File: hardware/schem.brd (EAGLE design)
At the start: 59.4 x 52.7 mm, 18 parts, among them IC1 7805L, IC2 L298, U2 TINY85-20-DIP

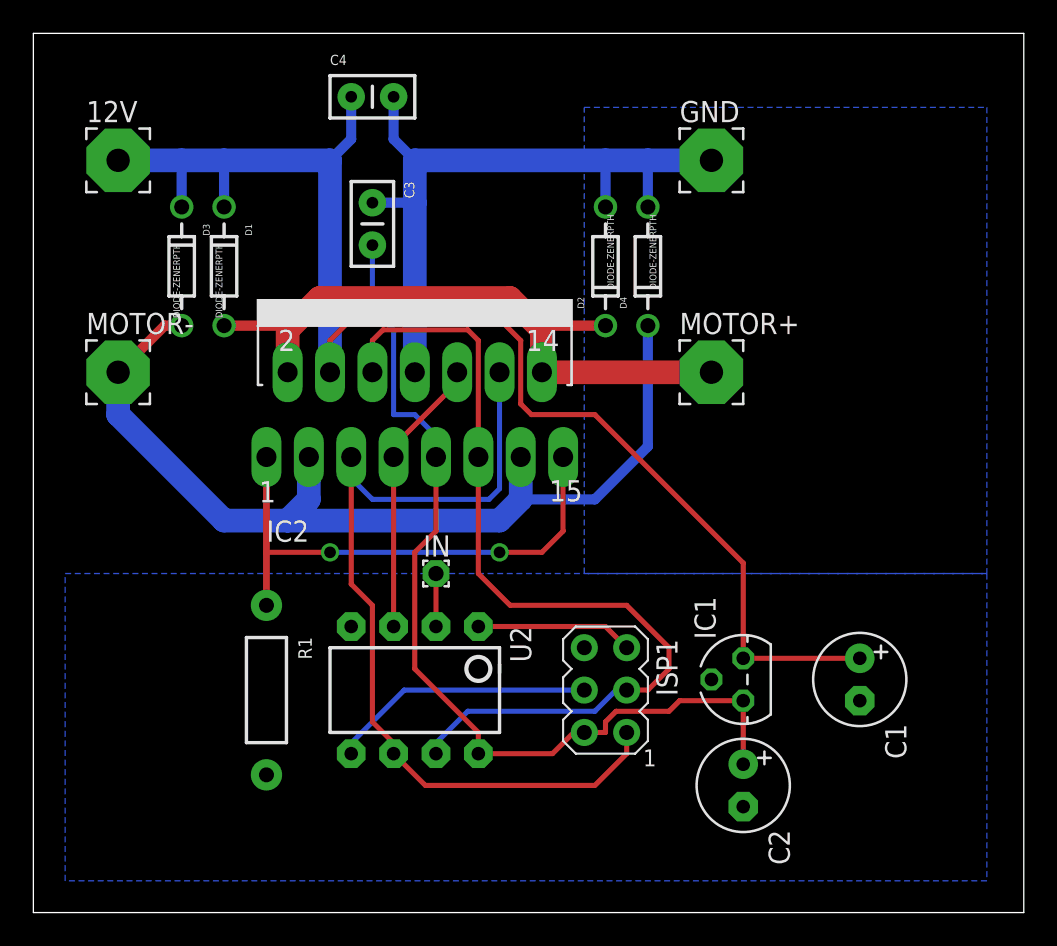
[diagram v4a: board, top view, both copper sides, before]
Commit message: Updated silk screen and moved components on board
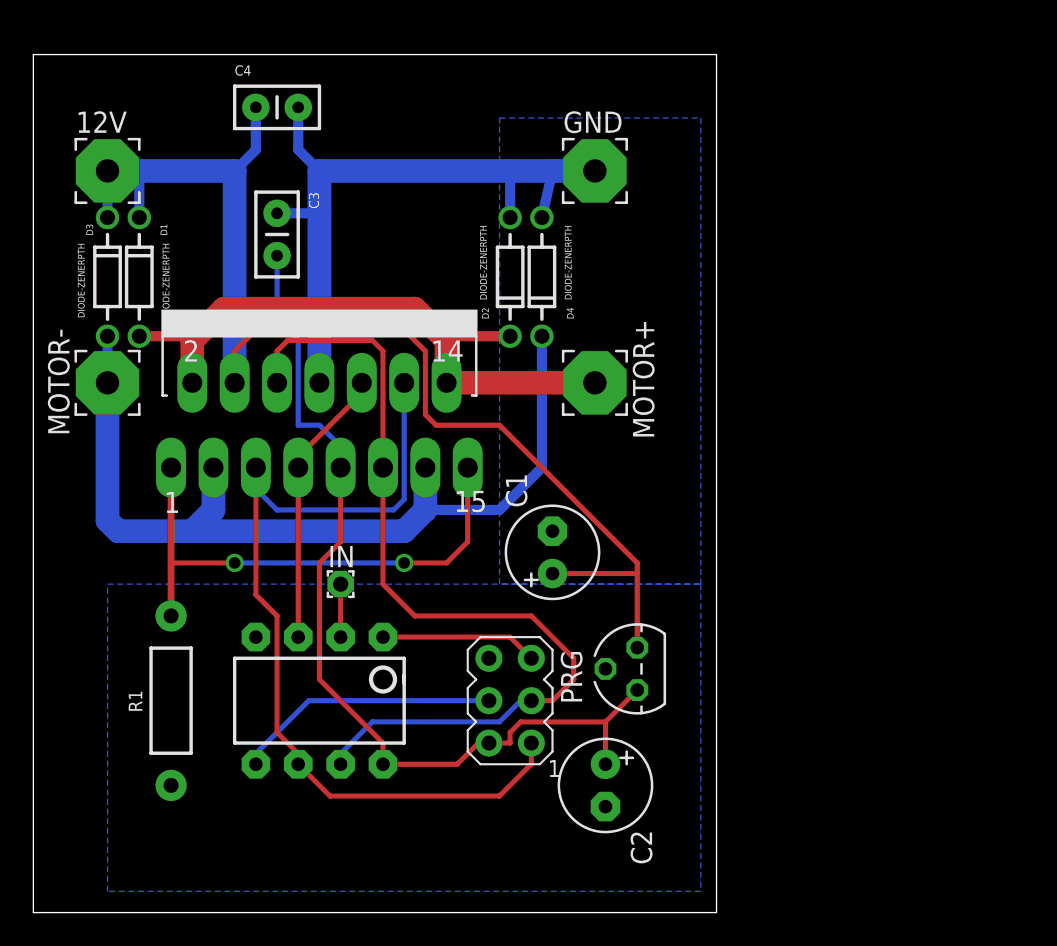
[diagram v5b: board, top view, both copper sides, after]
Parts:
- removed ISP1: AVRISP-6, adafruit:AVRISP
- added PRG: AVRISP-6, adafruit:AVRISP
- moved C1 19.9 mm to (31.1, 21.6), turned to 90 degrees
- moved C2 8.26 mm to (34.3, 7.62)
- moved GND 7.01 mm to (33.7, 44.5)
- moved MOTOR+ 7.01 mm to (33.7, 31.8)
- moved IC1 6.38 mm to (36.2, 14.6)
- moved D4 6.38 mm to (30.5, 38.1)
- moved C3 5.75 mm to (14.6, 41.9)
- moved C4 5.75 mm to (13.3, 48.3)
- moved D2 5.75 mm to (28.6, 38.1)
- moved IC2 5.75 mm to (17.1, 34.3)
- moved IN 5.75 mm to (18.4, 19.7)
- moved R1 5.75 mm to (8.26, 12.7)
- moved U2 5.75 mm to (17.1, 12.7)
- moved D1 5.12 mm to (6.35, 38.1)
- moved D3 4.49 mm to (4.45, 38.1)
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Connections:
- net +5V: now also PRG.2; no longer ISP1.2
- net GND: now also PRG.6; no longer ISP1.6
- net MISO: now also PRG.1; no longer ISP1.1
- net MOSI: now also PRG.4; no longer ISP1.4
- net RST: now also PRG.5; no longer ISP1.5
- net SCK: now also PRG.3; no longer ISP1.3
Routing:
- net +12V: track 83.5 -> 75.0 mm
- net OUT2: track 57.8 -> 53.7 mm
- net GND: track 73.4 -> 71.0 mm
- net OUT1: track 39.9 -> 38.0 mm
- net +5V: track 56.3 -> 54.9 mm
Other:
- board size 59.4 x 52.7 mm -> 40.9 x 51.4 mm

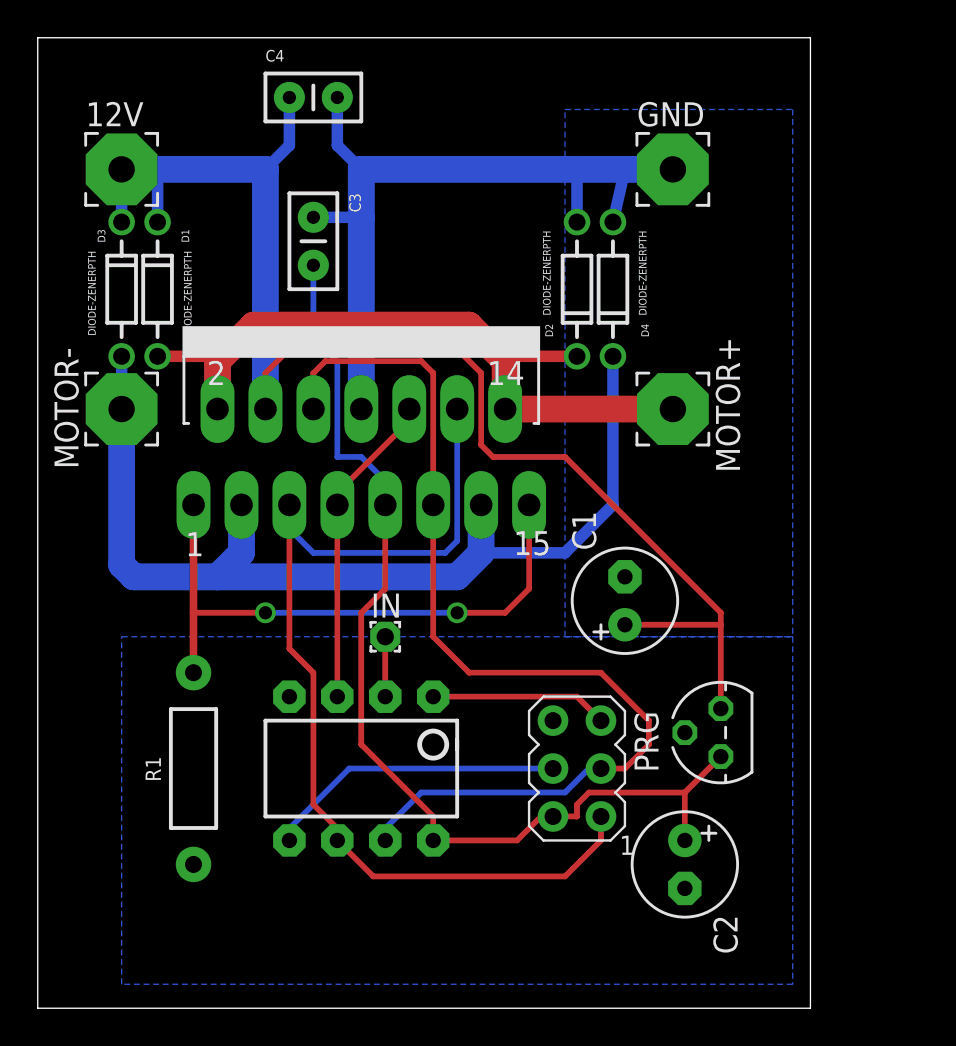
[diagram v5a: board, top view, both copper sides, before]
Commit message: Cleaned up board and moved around components
Made space to give H Bridge room to breath

Imporved Silk Screen
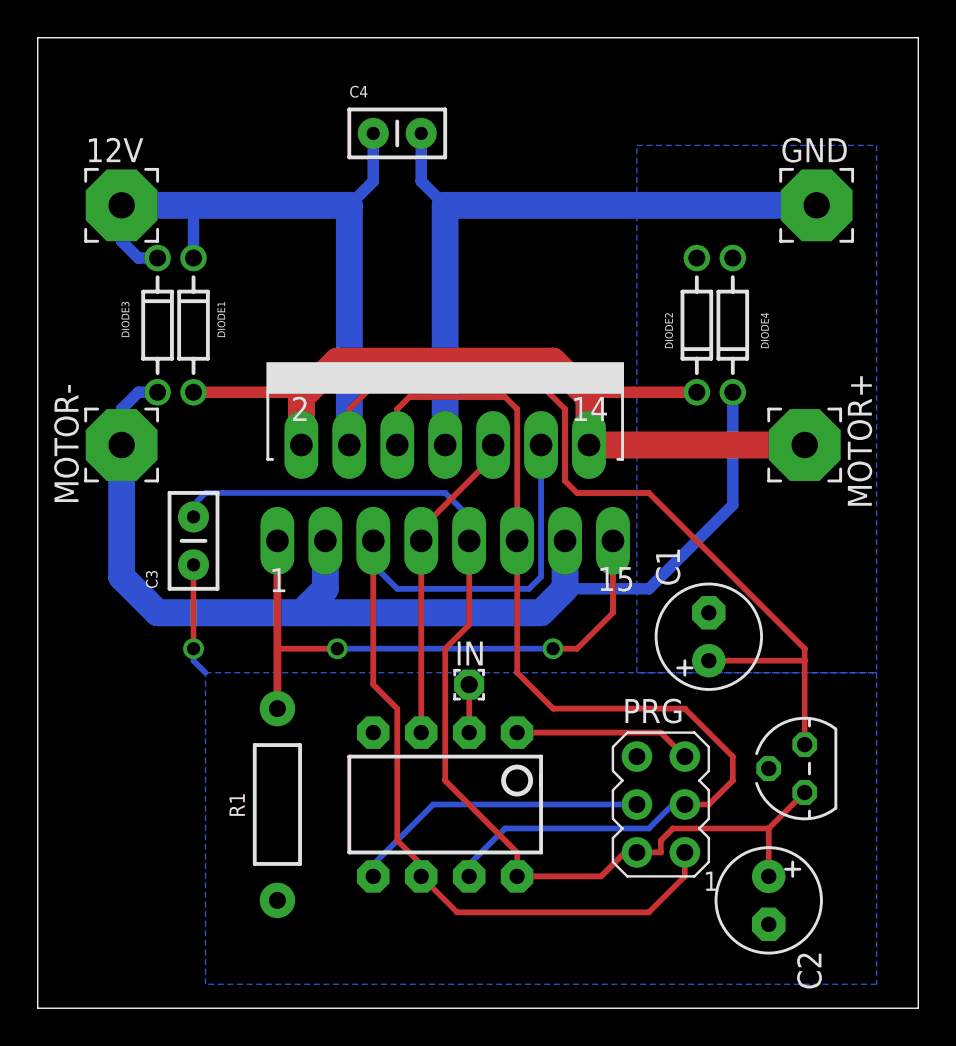
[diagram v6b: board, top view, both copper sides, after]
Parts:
- removed D1, D2, D3, D4: DIODE-ZENERPTH, SparkFun-DiscreteSemi:DIODE-ZENER
- added DIODE1, DIODE2, DIODE3, DIODE4: DIODE-ZENERPTH, SparkFun-DiscreteSemi:DIODE-ZENER
- moved C3 19.5 mm to (8.26, 23.5), turned to 90 degrees
- moved GND 7.85 mm to (41.3, 42.5)
- moved MOTOR+ 7.24 mm to (40.6, 29.8)
- moved IN 5.12 mm to (22.9, 17.1)
- moved C1 4.84 mm to (35.6, 19.7)
- moved PRG 4.84 mm to (33.0, 10.8)
- moved C2 4.84 mm to (38.7, 5.71)
- moved C4 4.84 mm to (17.8, 46.4)
- moved IC1 4.84 mm to (40.6, 12.7)
- moved IC2 4.84 mm to (21.6, 32.4)
- moved U2 4.84 mm to (21.6, 10.8)
- moved R1 4.84 mm to (12.7, 10.8)
- moved 12V 1.91 mm to (4.45, 42.5)
- moved MOTOR- 1.91 mm to (4.45, 29.8)
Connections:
- net +12V: now also DIODE1.P$1, DIODE3.P$1; no longer D1.P$1, D3.P$1
- net GND: now also DIODE2.P$2, DIODE4.P$2; no longer D2.P$2, D4.P$2
- net OUT1: now also DIODE1.P$2, DIODE2.P$1; no longer D1.P$2, D2.P$1
- net OUT2: now also DIODE3.P$2, DIODE4.P$1; no longer D3.P$2, D4.P$1
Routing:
- net GND: track 71.0 -> 42.7 mm, vias 0 -> 1
- net OUT1: track 38.0 -> 45.0 mm
- net OUT2: track 53.7 -> 59.5 mm
- net +12V: track 75.0 -> 80.2 mm
- net +5V: track 54.9 -> 57.2 mm
- net INP: track 3.17 -> 2.54 mm
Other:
- board size 40.9 x 51.4 mm -> 46.7 x 51.4 mm

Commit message: Improved ground plane
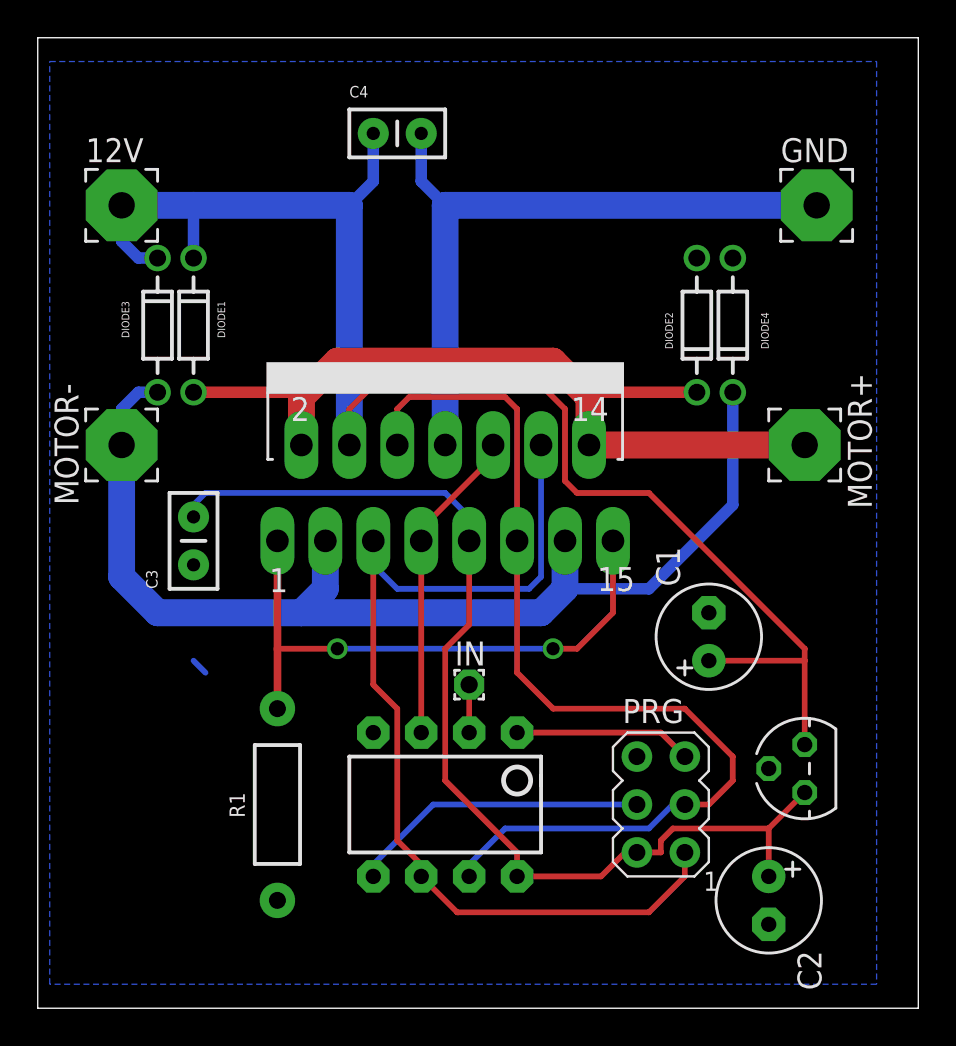
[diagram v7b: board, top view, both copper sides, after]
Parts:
- TINY85: value TINY85-20-DIP -> TINY85
- renumbered U2 to TINY85
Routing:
- net GND: track 42.7 -> 37.6 mm, vias 1 -> 0
- net +12V: track 80.2 -> 80.8 mm
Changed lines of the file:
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@@
 <attribute name="NAME" x="30.988" y="15.113" size="1.27" layer="25"/>
 </element>
-<element name="U2" library="SparkFun-DigitalIC" package="DIP08" value="TINY85-20-DIP" x="21.59" y="10.795" smashed="yes" rot="R180">
+<element name="TINY85" library="SparkFun-DigitalIC" package="DIP08" value="TINY85" x="21.59" y="10.795" smashed="yes" rot="R180">
 <attribute name="PROD_ID" value="IC-09445" x="-12.7" y="15.875" size="1.778" layer="27" rot="R180" display="off"/>
-<attribute name="VALUE" x="27.94" y="5.715" size="1.27" layer="27" ratio="10" rot="R180"/>
+<attribute name="VALUE" x="24.765" y="5.715" size="1.27" layer="27" ratio="10" rot="R180"/>
 </element>
 <element name="MOTOR+" library="wirepad" package="3,81/1,4" value="" x="40.64" y="29.845" smashed="yes">
@@
 <contactref element="DIODE3" pad="P$1"/>
 <contactref element="DIODE1" pad="P$1"/>
-<wire x1="4.445" y1="42.545" x2="16.51" y2="42.545" width="1.4224" layer="16"/>
+<wire x1="4.445" y1="42.545" x2="8.255" y2="42.545" width="1.4224" layer="16"/>
+<wire x1="8.255" y1="42.545" x2="16.51" y2="42.545" width="1.4224" layer="16"/>
 <wire x1="16.51" y1="42.545" x2="16.51" y2="29.845" width="1.4224" layer="16"/>
 <wire x1="17.78" y1="46.355" x2="17.78" y2="43.815" width="0.6096" layer="16"/>
@@
 <wire x1="5.334" y1="39.751" x2="4.445" y2="40.64" width="0.6096" layer="16"/>
 <wire x1="4.445" y1="40.64" x2="4.445" y2="42.545" width="0.6096" layer="16"/>
-<wire x1="8.255" y1="39.751" x2="8.255" y2="41.91" width="0.6096" layer="16"/>
-<wire x1="6.35" y1="39.751" x2="8.255" y2="39.751" width="0" layer="19" extent="1-1"/>
+<wire x1="8.255" y1="39.751" x2="8.255" y2="42.545" width="0.6096" layer="16"/>
 </signal>
 <signal name="GND">
@@
 <contactref element="C2" pad="-"/>
 <contactref element="PRG" pad="6"/>
-<contactref element="U2" pad="4"/>
+<contactref element="TINY85" pad="4"/>
 <contactref element="GND" pad="1"/>
 <contactref element="C3" pad="1"/>
@@
 <wire x1="20.32" y1="46.355" x2="20.32" y2="43.815" width="0.6096" layer="16"/>
 <wire x1="20.32" y1="43.815" x2="21.59" y2="42.545" width="0.6096" layer="16"/>
-<polygon width="0.3048" layer="16" isolate="0.3048">
-<vertex x="8.89" y="17.78"/>
-<vertex x="44.45" y="17.78"/>
+<polygon width="0.3048" layer="16" isolate="0.6096">
+<vertex x="0.635" y="50.165"/>
+<vertex x="44.45" y="50.165"/>
 <vertex x="44.45" y="1.27"/>
-<vertex x="8.89" y="1.27"/>
+<vertex x="0.635" y="1.27"/>
 </polygon>
-<polygon width="0.3048" layer="16" isolate="0.4064">
-<vertex x="31.75" y="45.72"/>
-<vertex x="44.45" y="45.72"/>
-<vertex x="44.45" y="17.78"/>
-<vertex x="31.75" y="17.78"/>
-</polygon>
-<wire x1="8.255" y1="23.495" x2="8.255" y2="19.05" width="0.3048" layer="1"/>
-<via x="8.255" y="19.05" extent="1-16" drill="0.7"/>
-<wire x1="8.255" y1="19.05" x2="8.255" y2="18.415" width="0.3048" layer="16"/>
 <wire x1="8.255" y1="18.415" x2="8.89" y2="17.78" width="0.3048" layer="16"/>
 </signal>
@@
 <contactref element="C2" pad="+"/>
 <contactref element="PRG" pad="2"/>
-<contactref element="U2" pad="8"/>
+<contactref element="TINY85" pad="8"/>
 <contactref element="IC2" pad="9"/>
 <contactref element="C3" pad="2"/>
@@
 </signal>
 <signal name="INP">
-<contactref element="U2" pad="2"/>
+<contactref element="TINY85" pad="2"/>
 <contactref element="IN" pad="1"/>
 <wire x1="22.86" y1="17.145" x2="22.86" y2="14.605" width="0.3048" layer="1"/>
@@
 <signal name="MOSI">
 <contactref element="PRG" pad="4"/>
-<contactref element="U2" pad="5"/>
+<contactref element="TINY85" pad="5"/>
 <wire x1="31.75" y1="10.795" x2="20.955" y2="10.795" width="0.3048" layer="16"/>
 <wire x1="20.955" y1="10.795" x2="17.78" y2="7.62" width="0.3048" layer="16"/>
@@
 </signal>
 <signal name="MISO">
-<contactref element="U2" pad="6"/>
+<contactref element="TINY85" pad="6"/>
 <contactref element="PRG" pad="1"/>
 <wire x1="34.29" y1="8.255" x2="34.29" y2="6.985" width="0.3048" layer="1"/>
@@
 </signal>
 <signal name="RST">
-<contactref element="U2" pad="1"/>
+<contactref element="TINY85" pad="1"/>
 <contactref element="PRG" pad="5"/>
 <wire x1="25.4" y1="14.605" x2="33.02" y2="14.605" width="0.3048" layer="1"/>
@@
 <signal name="SCK">
 <contactref element="PRG" pad="3"/>
-<contactref element="U2" pad="7"/>
+<contactref element="TINY85" pad="7"/>
 <wire x1="34.29" y1="10.795" x2="33.655" y2="10.795" width="0.3048" layer="16"/>
 <wire x1="33.655" y1="10.795" x2="32.385" y2="9.525" width="0.3048" layer="16"/>
@@
 </signal>
 <signal name="IN2">
-<contactref element="U2" pad="3"/>
+<contactref element="TINY85" pad="3"/>
 <contactref element="IC2" pad="10"/>
 <contactref element="IC2" pad="7"/>
